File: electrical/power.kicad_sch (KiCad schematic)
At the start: 61 parts

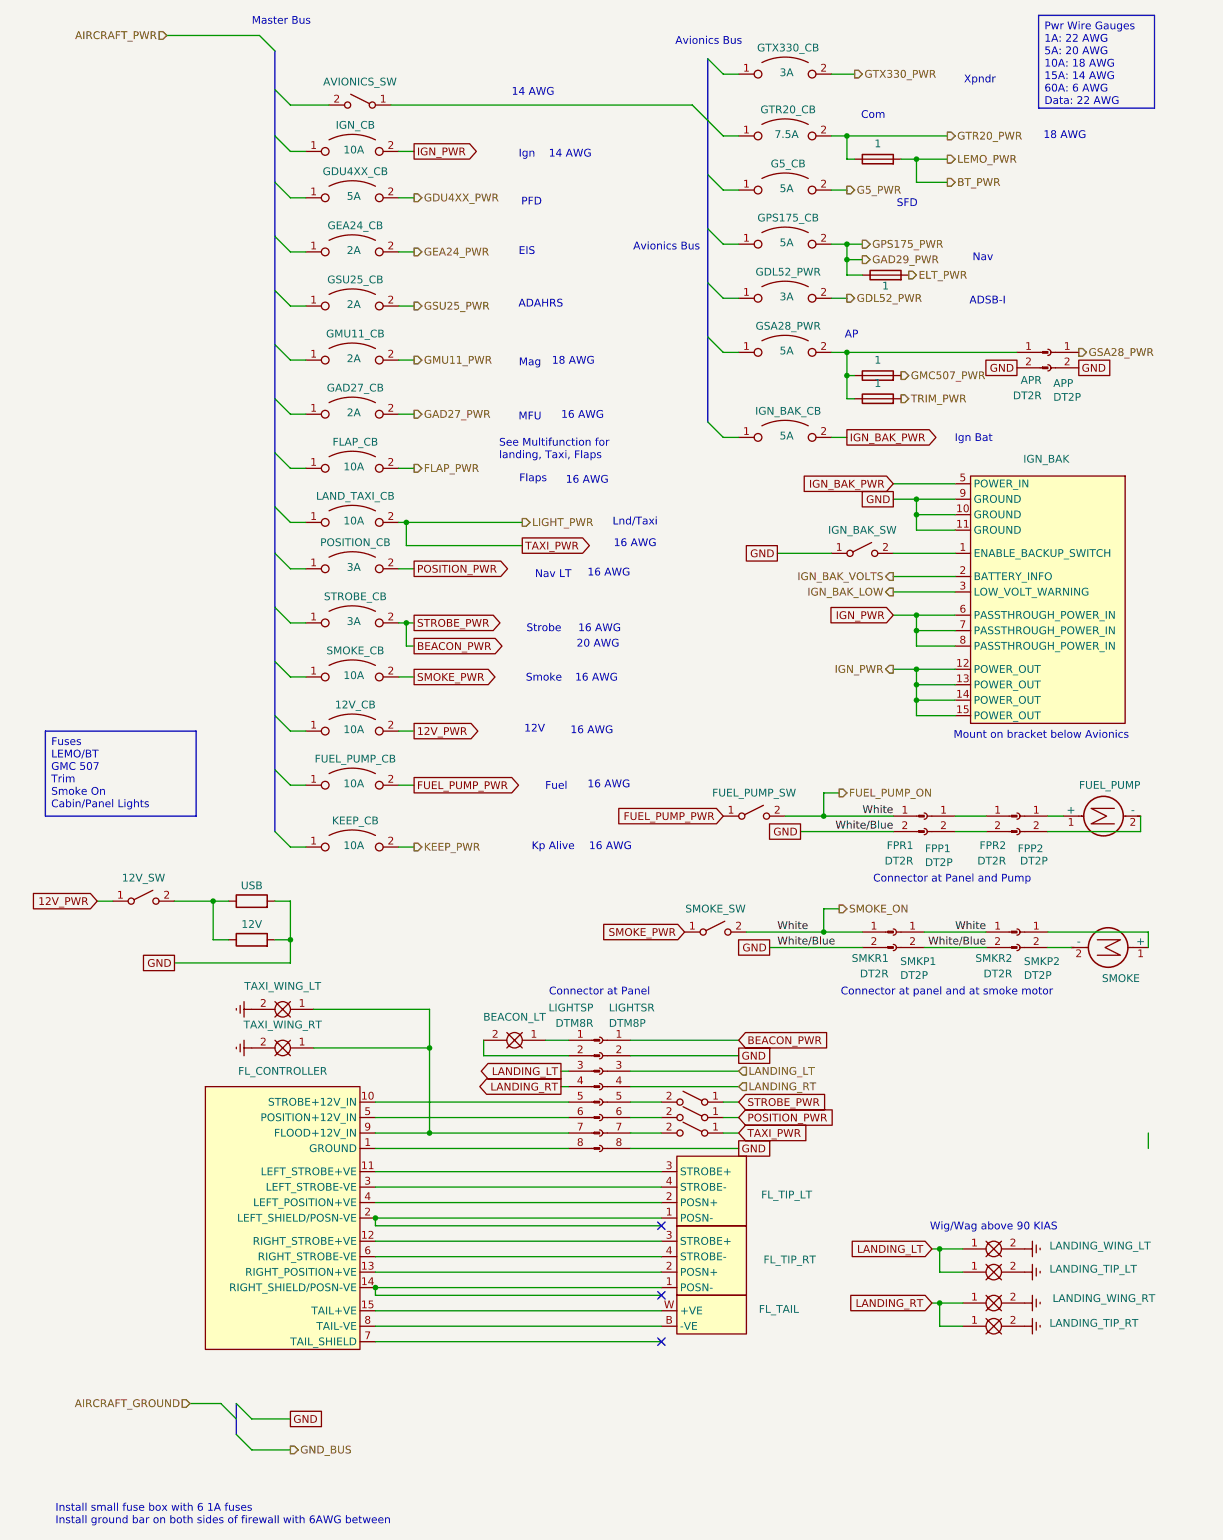
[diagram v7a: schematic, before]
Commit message: Assumed engine connector is sufficient for wiring on bench..
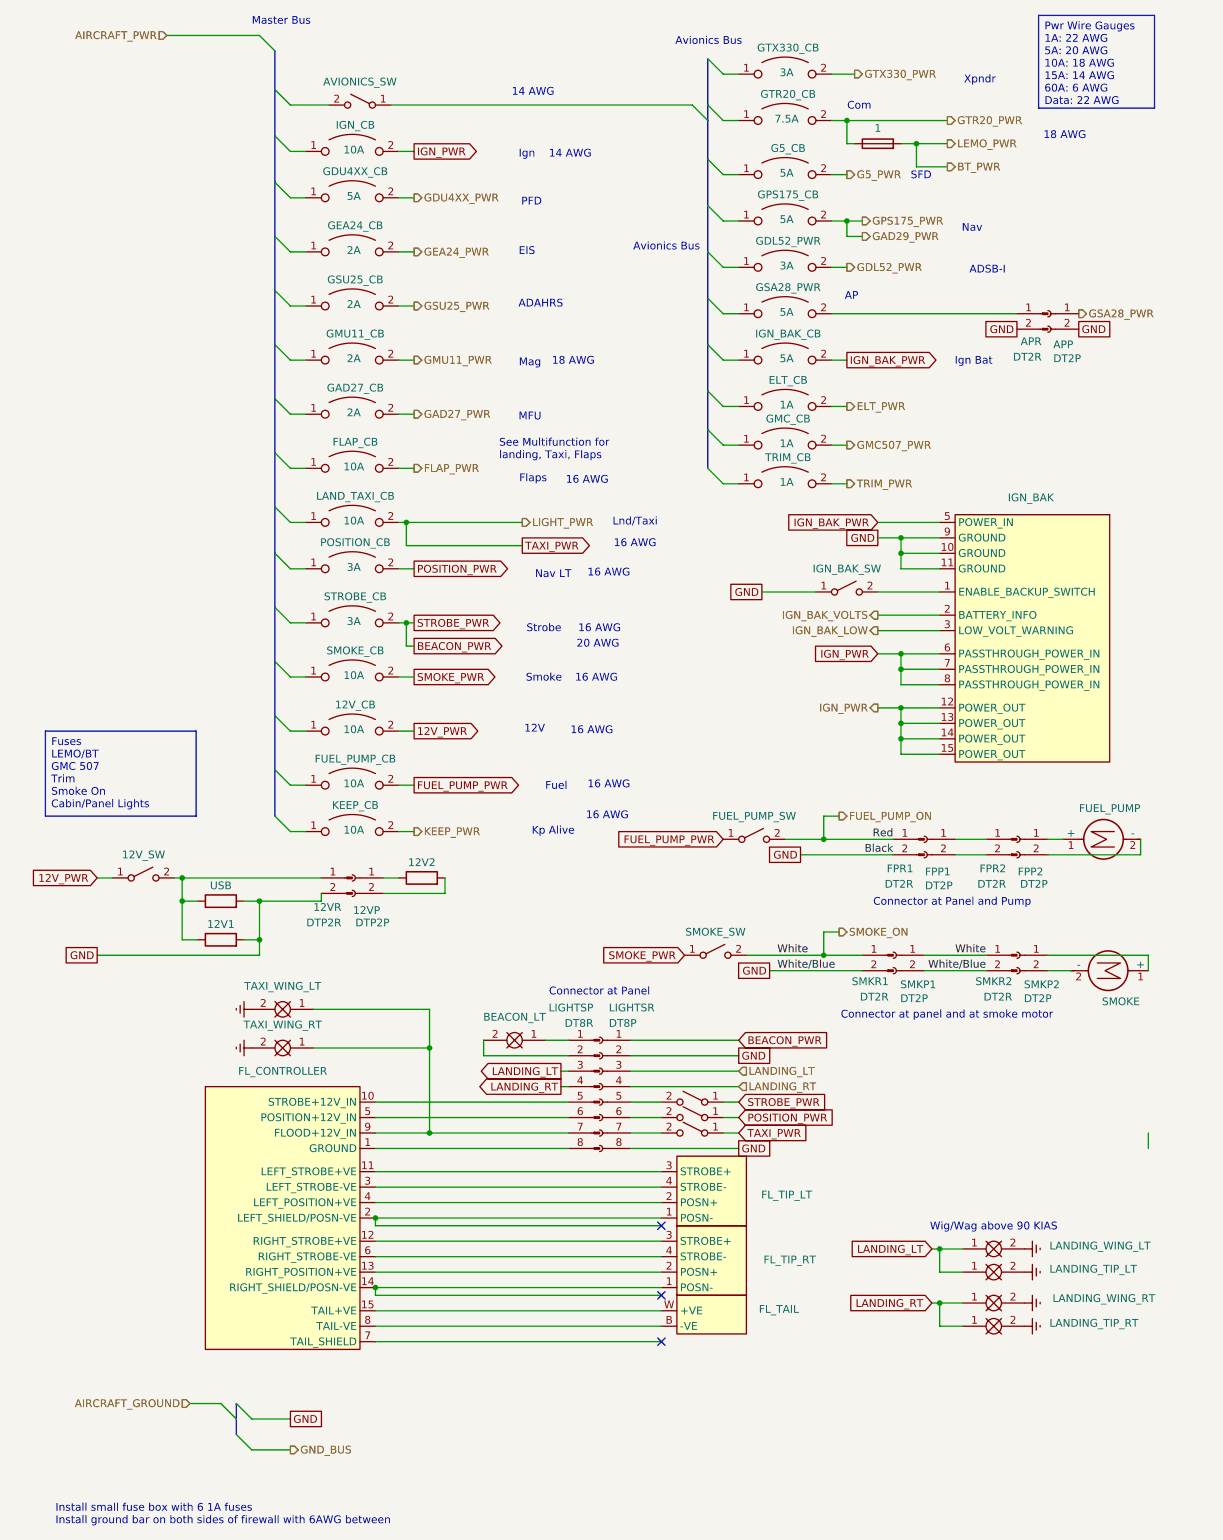
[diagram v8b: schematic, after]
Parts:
- removed GMC507_FS, GMC507_FS1, LEMO_FS1: 1, symbol Device:Fuse
- added 12V2: R, symbol Device:R
- added 12VP: DTP2P, symbol Connector:Conn_01x02_Socket
- added 12VR: DTP2R, symbol Connector:Conn_01x02_Pin
- added ELT_CB, GMC_CB, TRIM_CB: 1A, symbol Device:CircuitBreaker_1P_US
- LIGHTSP: value DTM8R -> DT8R
- LIGHTSR: value DTM8P -> DT8P
- renumbered 12V to 12V1
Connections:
- net ELT_PWR: now also ELT_CB.2
- net FUEL_PUMP_ON: no longer SMKP1.1 (Pin_1), SMKR1.1 (Pin_1), SMKR2.1 (Pin_1), SMOKE_SW.2 (B)
- net GMC507_PWR: now also GMC_CB.2
- net GND: now also 12VR.2 (Pin_2)
- net TRIM_PWR: now also TRIM_CB.2
- net at 12V1.1, 12V_SW.2 (B), USB.1: now also 12VR.1 (Pin_1)
- new net: 12V2.1, 12VP.1 (Pin_1)
- new net: 12V2.2, 12VP.2 (Pin_2)
- new net SMOKE_ON: SMKP1.1 (Pin_1), SMKR1.1 (Pin_1), SMKR2.1 (Pin_1), SMOKE_SW.2 (B)
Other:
- note removed: "Mount on bracket below Avionics"
- moved on the sheet: 12V1, 12V_SW, APP, APR, FPP1, FPP2, FPR1, FPR2, FUEL_PUMP, FUEL_PUMP_SW, G5_CB, GDL52_PWR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
